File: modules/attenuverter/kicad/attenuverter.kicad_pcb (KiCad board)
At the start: 2 copper layers, 28 x 108 mm, 23 parts, among them J1 IN 1, J2 OUT 1, J3 IN 2, J4 OUT 2, J5 POWER, U1 TL072

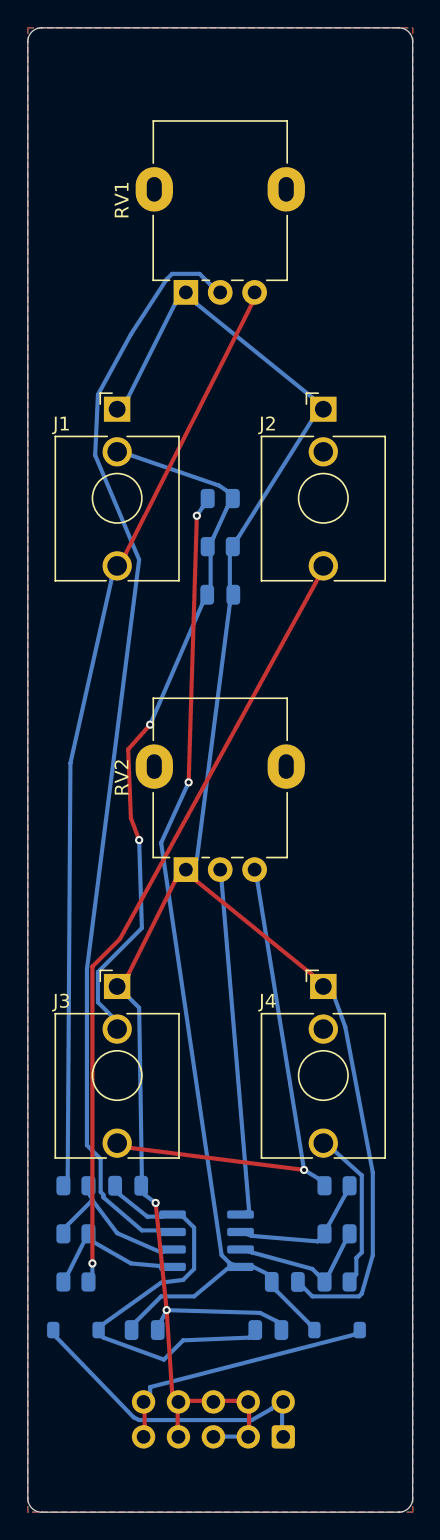
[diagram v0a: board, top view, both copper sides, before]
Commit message: Router: charge history congestion in the same currency as present congestion
Chasing the via-count gap Freerouting exposed found a defect in our
implementation of negotiated congestion, not a mistuned via cost.

Present congestion grew as 1.4^round while history congestion accumulated a
flat +1 per round, so by round 200 the present term was about 1e29 and history
at most 200. History was arithmetically irrelevant, the negotiation had no
memory, and two nets in conflict simply traded places forever. McMurchie &
Ebeling's convergence argument needs a cell that has been fought over to stay
expensive after it falls free.

Found by sweeping the via cost from 10 to 320 over every benchmark board:
legality flipped on and off as the cost moved (reversal legal at 25 and 40,
illegal at 15, 30 and 320), and ten times the negotiation budget fixed
neither failing cost. A stall, not slow convergence.

History is now charged +pres per round. The exponent is capped at 500 because
1.4^2100 overflows a Double to infinity, which would poison every cost in the
penalty array.

Results:
- the sweep goes from 11 of 17 legal to 24 of 24; every via cost from 10 to
  320 converges on every board
- route-test at the unchanged default via cost: 27 vias and 717.67 mm become 7
  vias and 698.69 mm, against Freerouting's 6 vias and 690.79 mm, so the via
  gap closes from 4.5x to 1.17x and the copper gap from 3.9% to 1.1%
- the one remaining reversal failure now responds to budget, which is what the
  algorithm promises and previously did not; the default budget goes from 200
  to 600, and since the loop exits as soon as nothing is contested, boards that
  settle early pay nothing for it

The via cost stays at 40. After the fix no value is undominated everywhere:
40 gives the fewest vias on route-test and is beaten on both axes by 25 and 30
on the attenuverter and on reversal, while 20 wins route-test and then spends
51 vias on reversal where 25 spends 9. Too wide a spread to tune against five
bo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
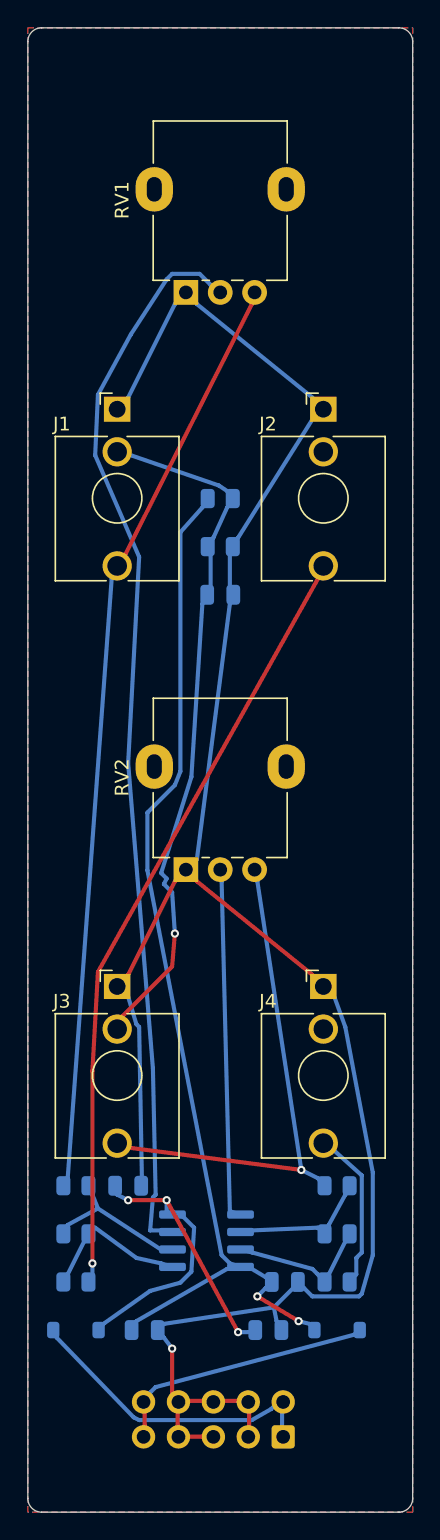
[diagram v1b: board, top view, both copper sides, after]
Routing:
- net GND: track 167.0 -> 158.7 mm, vias 2 -> 1
- net /WIPER1: track 80.1 -> 77.7 mm
- net +12V: track 75.0 -> 77.1 mm
- net /OFFSET: track 51.8 -> 50.9 mm, vias 2 -> 1
- net -12V: track 31.4 -> 31.1 mm, vias 0 -> 3

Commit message: Net order dominates the router; measure what analog layout actually binds
Two threads, both driven by measurement rather than by assumption.

## The router: ordering beats every other setting

The via-cost spread left over from the last session was path dependence, not
noise. The negotiation only reroutes nets that are in conflict, so a net that
took a wasteful path in round one and was never contested again keeps it to
the end, and final quality follows the order conflicts happened to appear in.

Two changes. A post-convergence descent (rcImproveRounds) offers every net one
more route against the others' finished copper and keeps it only when it is
cheaper by the measure the A* itself minimises, so total cost strictly
decreases and it terminates. And multi-start (rcStarts): the negotiation runs
once per net ordering and the best result is kept, lexicographically on faults,
then contested cells, then cost, never a weighted sum. The orderings are four
named heuristics -- most terminals first, fewest first, longest span first,
shortest first -- and then deterministic shuffles; hardest-first against
easiest-first is a real disagreement in the literature and neither wins on
every board, which is the argument for running both.

Measured at the default via cost over the three congested boards:

  starts | reversal            | route-test | attenuverter
  1      | illegal, 202 vias   | 30 vias    | 9 vias
  2      | illegal             | 17 vias    | 7 vias
  4      | 23 vias             |  9 vias    | 5 vias
  6      | 14 vias             |  9 vias    | 5 vias
  8      | identical to 6      | identical  | identical

A single ordering leaves the crossing fixture illegal with 202 vias; six get
it to 14. Nothing else in the router buys a factor of fourteen, and the curve
is flat past six. The descent is separately worth one or two vias, and needed
its conflict test fixed: contest is symmetric, and checking only "my new
copper in someone else's halo" accepted reroutes that sw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
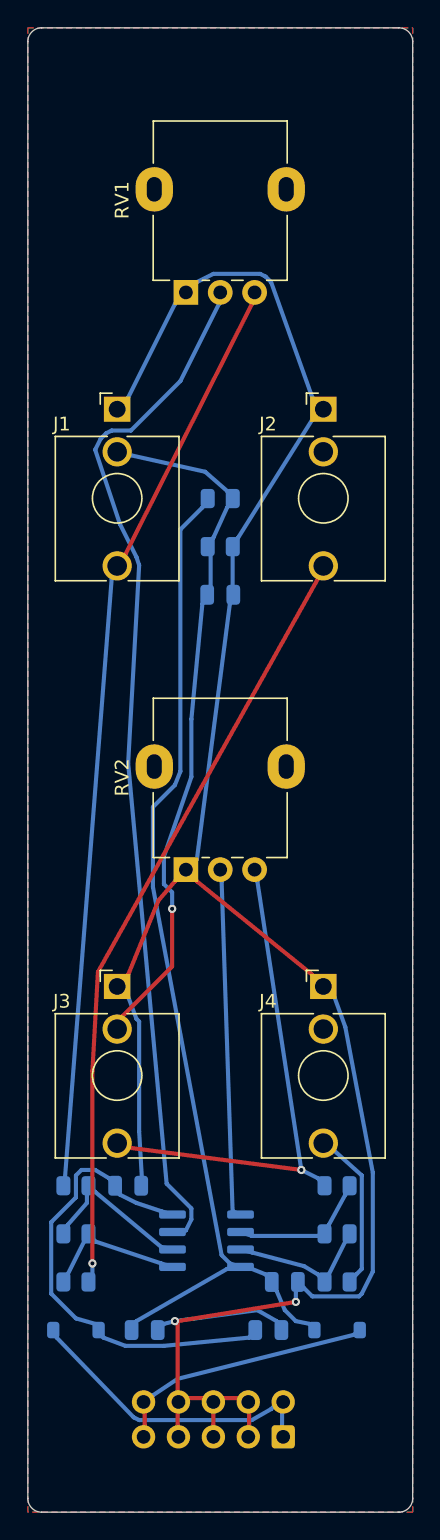
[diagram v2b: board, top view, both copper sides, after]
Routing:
- net GND: track 158.7 -> 170.1 mm, vias 1 -> 2
- net -12V: track 31.1 -> 34.2 mm, vias 3 -> 0
- net /WIPER1: track 77.7 -> 74.9 mm
- net +12V: track 77.1 -> 75.6 mm, vias 2 -> 0
- net /INV1: track 11.3 -> 11.9 mm

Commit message: Attenuverter option B: precision circuit, models, eight decks, 100 mm boards
The attenuverter becomes the option B design the user chose: one OPA2197
per channel as unity-gain input buffer plus attenuverter stage, 10k 0.1%
thin-film gain resistors with 10 pF C0G compensation, a 1M input and a
REF5050 offset reference. OPA2197 and REF5050 models are built from the
datasheet maxima with input capacitance, a second pole and TEMPER terms.
Emit.Spice learns Reference_Voltage symbols and places a 0 V probe in every
op-amp output so a deck can measure loop gain by voltage injection on the
generated netlist. Eight decks assert every limit in the error budget and
pass: the stage has 72 degrees of phase margin with the capacitor and 27
without; the gain resistors are 10k rather than the assumed 100k because
the input capacitance shelved the full-clockwise response 4.6 % at 20 kHz
with 100k. eurorackPcbHeight drops to 100 mm for every module; the
attenuverter's SMD moves into the pad-free strips between its controls.
65 tests, both pipelines and sim.sh pass; the decision file is retired
into SPEC.md.

Co-Authored-By: Claude Fable 5.1 <noreply@anthropic.com>
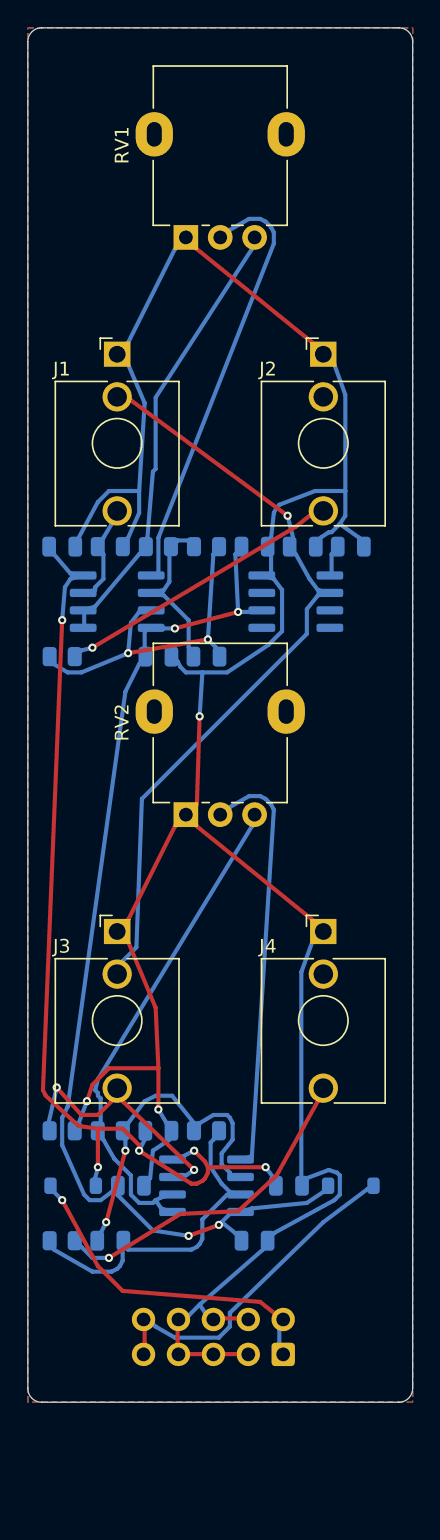
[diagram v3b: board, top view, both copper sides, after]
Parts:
- removed C5: 100n, Capacitor_SMD:C_0805_2012Metric
- removed R7: 1.5k, Resistor_SMD:R_0805_2012Metric
- removed R8: 1k, Resistor_SMD:R_0805_2012Metric
- added C10: 10p, Capacitor_SMD:C_0805_2012Metric, B.Cu at (6.00, 88.2)
- added C11: 100n, Capacitor_SMD:C_0805_2012Metric, B.Cu at (16.5, 88.2)
- added C12: 100n, Capacitor_SMD:C_0805_2012Metric, B.Cu at (9.50, 80.2)
- added C6: 1u, Capacitor_SMD:C_0805_2012Metric, B.Cu at (16.5, 37.8)
- added C7: 1u, Capacitor_SMD:C_0805_2012Metric, B.Cu at (20.0, 37.8)
- added C8: 1u, Capacitor_SMD:C_0805_2012Metric, B.Cu at (23.5, 37.8)
- added C9: 10p, Capacitor_SMD:C_0805_2012Metric, B.Cu at (13.0, 45.8)
- added R10: 1M, Resistor_SMD:R_0805_2012Metric, B.Cu at (2.50, 80.2)
- added R9: 1M, Resistor_SMD:R_0805_2012Metric, B.Cu at (6.00, 37.8)
- added U2: OPA2197, Package_SO:SOIC-8_3.9x4.9mm_P1.27mm, B.Cu at (13.0, 84.2)
- added U3: REF5050, Package_SO:SOIC-8_3.9x4.9mm_P1.27mm, B.Cu at (19.5, 41.8)
- R1, R2, R4, R5: value 100k -> 10k
- U1: value TL072 -> OPA2197
- moved R2 50.9 mm to (13.0, 37.8)
- moved U1 47.0 mm to (6.50, 41.8)
- moved R1 46.9 mm to (9.50, 37.8)
- moved C4 46.7 mm to (2.50, 37.8)
- moved C3 46.4 mm to (9.50, 45.8)
- moved R3 45.5 mm to (2.50, 45.8)
- moved R6 20.2 mm to (2.50, 88.2)
- moved R4 17.0 mm to (6.00, 80.2)
- moved R5 12.1 mm to (13.0, 80.2)
- moved C2 10.6 mm to (19.0, 84.2)
- moved C1 10.5 mm to (7.50, 84.2)
- moved D2 10.5 mm to (23.5, 84.2)
- moved D1 10.5 mm to (3.30, 84.2)
- moved J5 6.00 mm to (18.6, 96.5)
- moved J1 4.00 mm to (6.50, 23.8)
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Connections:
- R1 pad 1: /IN1 -> /BUF1
- R4 pad 1: /IN2 -> /BUF2
- RV1 pad 3: /IN1 -> /BUF1
- RV2 pad 3: /IN2 -> /BUF2
- U1 pad 1: /OA1 -> /BUF1
- U1 pad 2: /INV1 -> /BUF1
- U1 pad 3: /WIPER1 -> /IN1
- U1 pad 5: /WIPER2 -> /WIPER1
- U1 pad 6: /INV2 -> /INV1
- U1 pad 7: /OA2 -> /OA1
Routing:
- net /IN1: track 67.6 -> 7.40 mm
- net /WIPER1: track 74.9 -> 31.7 mm
- net -12V: track 34.2 -> 72.0 mm, vias 0 -> 5
- net /BUF2: track 0.00 -> 36.9 mm
- net /OUT1: track 56.4 -> 21.0 mm
- net /BUF1: track 0.00 -> 32.6 mm
- net GND: track 170.1 -> 201.7 mm, vias 2 -> 3
- net /IN2: track 37.8 -> 19.5 mm, vias 1 -> 2
- net /INV2: track 10.1 -> 24.9 mm, vias 0 -> 2
- net /OA2: track 10.6 -> 25.4 mm
- net /OA1: track 10.6 -> 24.9 mm, vias 0 -> 2
- net /OUT2: track 11.8 -> 24.3 mm, vias 0 -> 1
- net /OFFSET: track 50.8 -> 56.4 mm
- net /WIPER2: track 25.5 -> 30.9 mm
- net /P12_RAW: track 19.3 -> 24.5 mm
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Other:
- board size 28 x 108 mm -> 28 x 100 mm

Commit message: Factor power entry and protection into Block.Power
The 2x5 shrouded IDC header, the series B5819W Schottkys and the 10 uF bulk
capacitors, with the five nets they define, become Block.Power: the block
fixes what each part is (value, symbol, footprint, LCSC number, who
installs it) and the design supplies a Placed record per part saying where
it goes. Design gains Placed and mergeNets, which joins the GND, +12V and
-12V fragments a block contributes with the design's own by name, leaving a
same-name kind clash for validation to reject. The attenuverter is the
first consumer.

Acceptance: the regenerated schematic is identical to the previous one up
to the order of the five power symbols (zero differing lines when both are
sorted); the board differs because the changed pad order changed the
router's tie-breaks, and its report shows an equivalent solution (745 mm
of copper against 752, 23 vias against 22, detour 1.17 against 1.18, no
contested cells, no analog findings). Module and panel pass ERC and DRC
with schematic parity, the eight decks pass, 78/78 tests pass.

Co-Authored-By: Claude Fable 5.1 <noreply@anthropic.com>
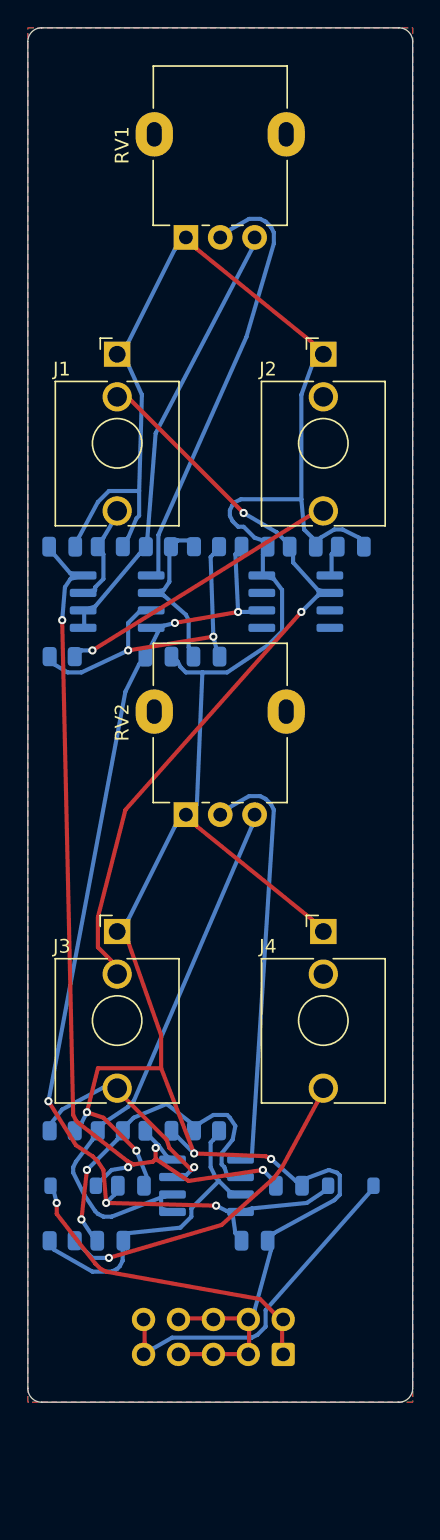
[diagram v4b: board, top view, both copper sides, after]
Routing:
- net /BUF2: track 36.9 -> 41.5 mm
- net -12V: track 72.0 -> 68.0 mm, vias 5 -> 4
- net /IN2: track 19.5 -> 16.5 mm, vias 2 -> 1
- net /OA2: track 25.4 -> 23.0 mm
- net GND: track 201.7 -> 199.6 mm, vias 3 -> 4
- net /P12_RAW: track 24.5 -> 25.2 mm
- net /OFFSET: track 56.4 -> 56.2 mm, vias 1 -> 2
- net +12V: vias 4 -> 5
